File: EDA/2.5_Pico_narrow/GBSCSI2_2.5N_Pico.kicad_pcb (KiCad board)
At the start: 4 copper layers, 69.5 x 93.5 mm, 109 parts, among them J1 SCSI_50-2P_2mm, J1.1 SCSI_50P_2.54mm, J2 TF003, J5 Conn_01x04, J6 Conn_01x02, Q1 AO3401A, Q10 AO3401A, Q11 AO3401A, Q12 AO3401A, Q13 AO3401A, Q14 AO3401A, Q15 AO3401A, Q16 AO3401A, Q17 AO3401A, Q18 AO3401A, Q2 AO3401A, Q3 AO3401A, Q4 AO3401A, Q5 AO3401A, Q6 AO3401A, Q7 AO3401A, Q8 AO3401A, Q9 AO3401A, SW1 SW_DIP_x03, U1 Pico(2(W)), U10 AZ1117-2.85, U4 74LVTH245, U5 74LVTH245, U6 74LVTH125, U7 74LVTH125, U8 SN74AHC1G125DBVR, U9 TLV62569DBV

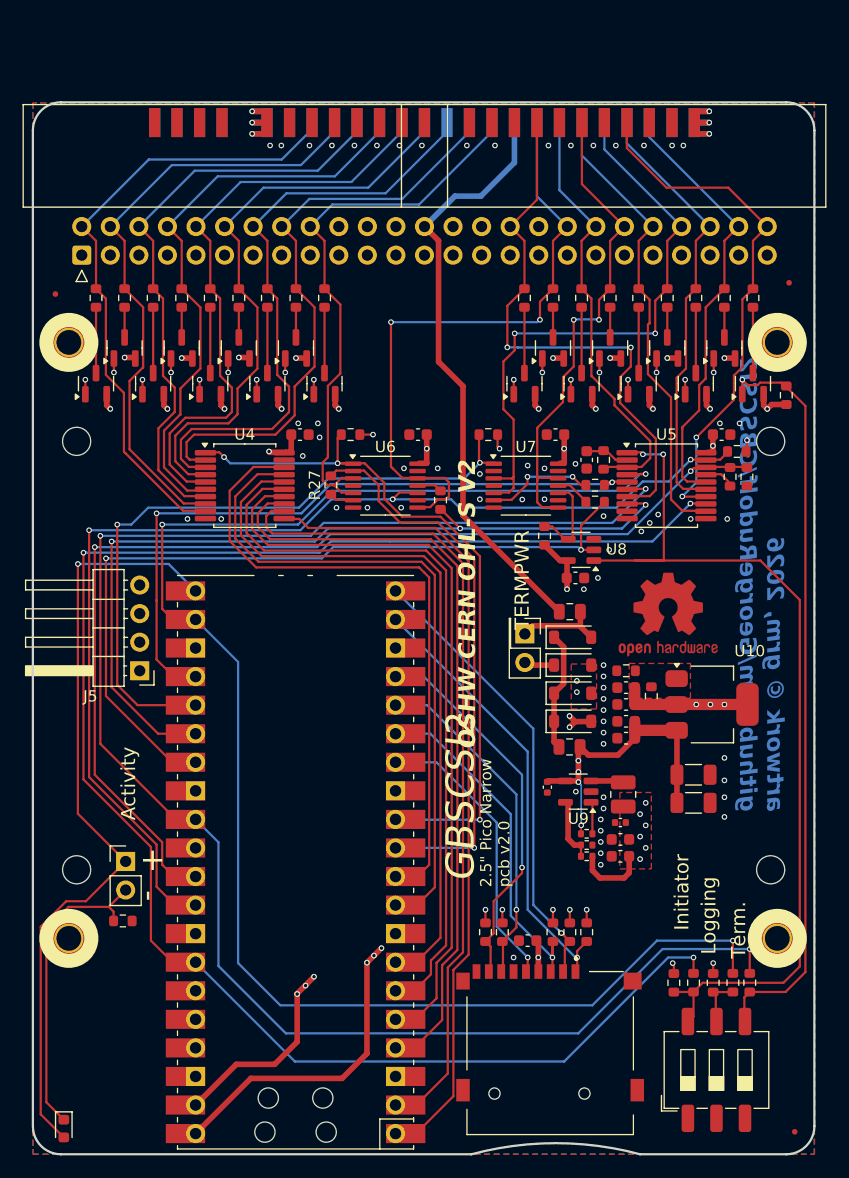
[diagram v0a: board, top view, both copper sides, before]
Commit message: Tidying up PCB footprint slightly, more work needed, ERC passes on narrow variants
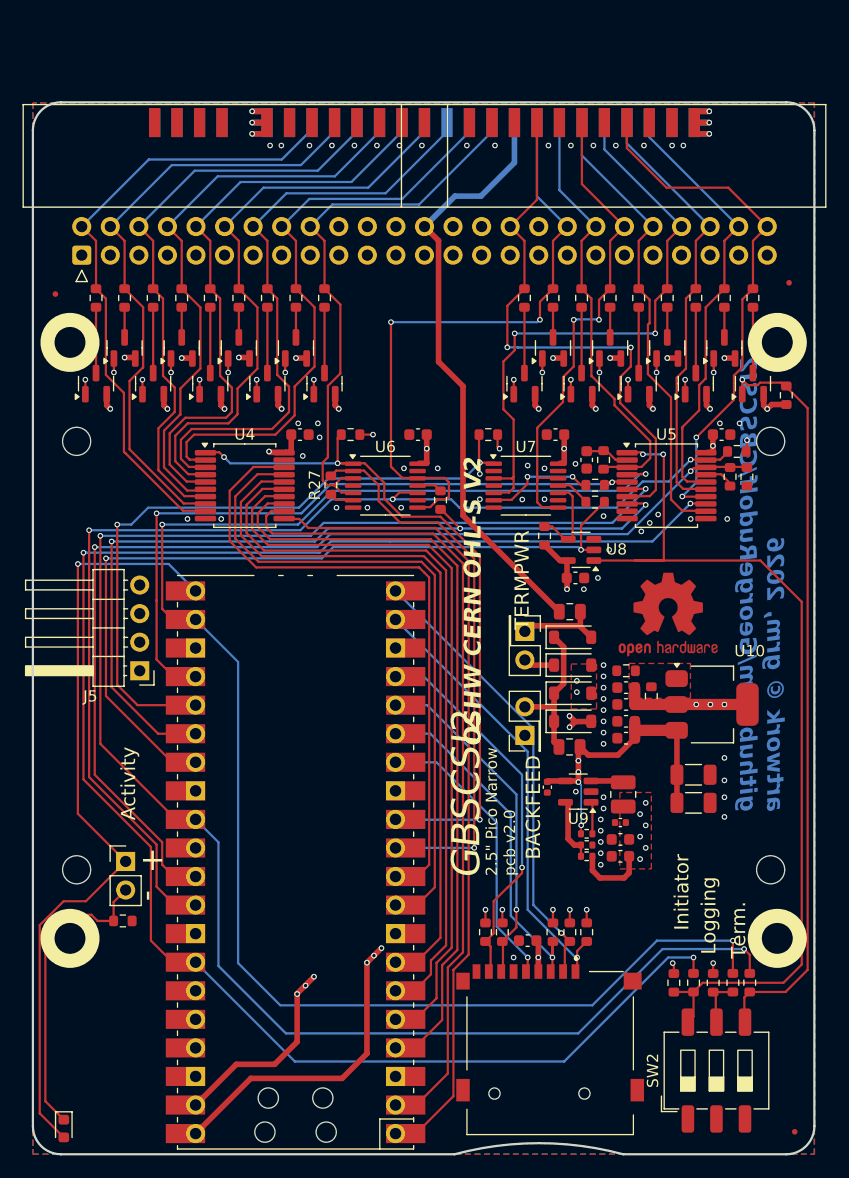
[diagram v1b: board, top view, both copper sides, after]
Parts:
- removed SW1: SW_DIP_x03, Button_Switch_SMD:SW_DIP_SPSTx03_Slide_6.7x9.18mm_W8.61mm_P2.54mm_LowProfile
- added JP2: Jumper_2_Open, Connector_PinHeader_2.54mm:PinHeader_2x01_P2.54mm_Vertical, F.Cu at (79.2, 105.2)
- added SW2: SW_DIP_x03, Button_Switch_SMD:SW_DIP_SPSTx03_Slide_6.7x9.18mm_W8.61mm_P2.54mm_LowProfile, F.Cu at (96.3, 135.1)
- R10, R11, R12, R5, R6, R8, R9: value 4k7 -> 4.7kΩ
- moved JP1 0.22 mm to (79.2, 96.0)
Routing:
- net +5VIN: track 282.0 -> 291.1 mm
- net /Power/5V_TIE: track 10.6 -> 13.3 mm
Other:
- outline, holes or cut-outs redrawn
- board text added: "BACKFEED"

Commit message: Prettifying models
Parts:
- moved C20 7.00 mm to (94.2, 104.2)
- moved C21 7.00 mm to (84.8, 73.8)
- moved C22 7.00 mm to (59.2, 71.5)
- moved C23 7.00 mm to (96.8, 71.5)
- moved C24 7.00 mm to (83.8, 84.2)
- moved C25 7.00 mm to (69.8, 71.5)
- moved C26 7.00 mm to (82.0, 71.5)
- moved C27 7.00 mm to (81.2, 102.9)
- moved C28 7.00 mm to (87.8, 106.0)
- moved C29 7.00 mm to (87.8, 109.0)
- moved C30 7.00 mm to (87.8, 107.5)
- moved C31 7.00 mm to (88.2, 98.5)
- moved C32 7.00 mm to (88.2, 97.0)
- moved C33 7.00 mm to (88.2, 95.5)
- moved C34 7.00 mm to (88.2, 94.0)
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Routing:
- net +5VIN: track 291.1 -> 181.3 mm
- net +2.8V: track 192.5 -> 181.3 mm
- net GND: track 0.00 -> 7.85 mm
- net /Core Logic, Basic Controls/~{MCU_REQ}: track 140.2 -> 144.5 mm
- net VBUS: track 76.8 -> 78.6 mm
- net /Core Logic, Basic Controls/SDIO_D3: track 40.4 -> 42.0 mm
- net /Core Logic, Basic Controls/~{MCU_IO}: track 150.1 -> 149.1 mm
- net /Core Logic, Basic Controls/~{MCU_ATTN}: track 152.3 -> 153.1 mm
- added copper zone on B.Cu, net +3.3V
- added copper zone on In2.Cu, net GND
- removed copper zone on In2.Cu, net +3.3V
- removed copper zone on B.Cu, net GND

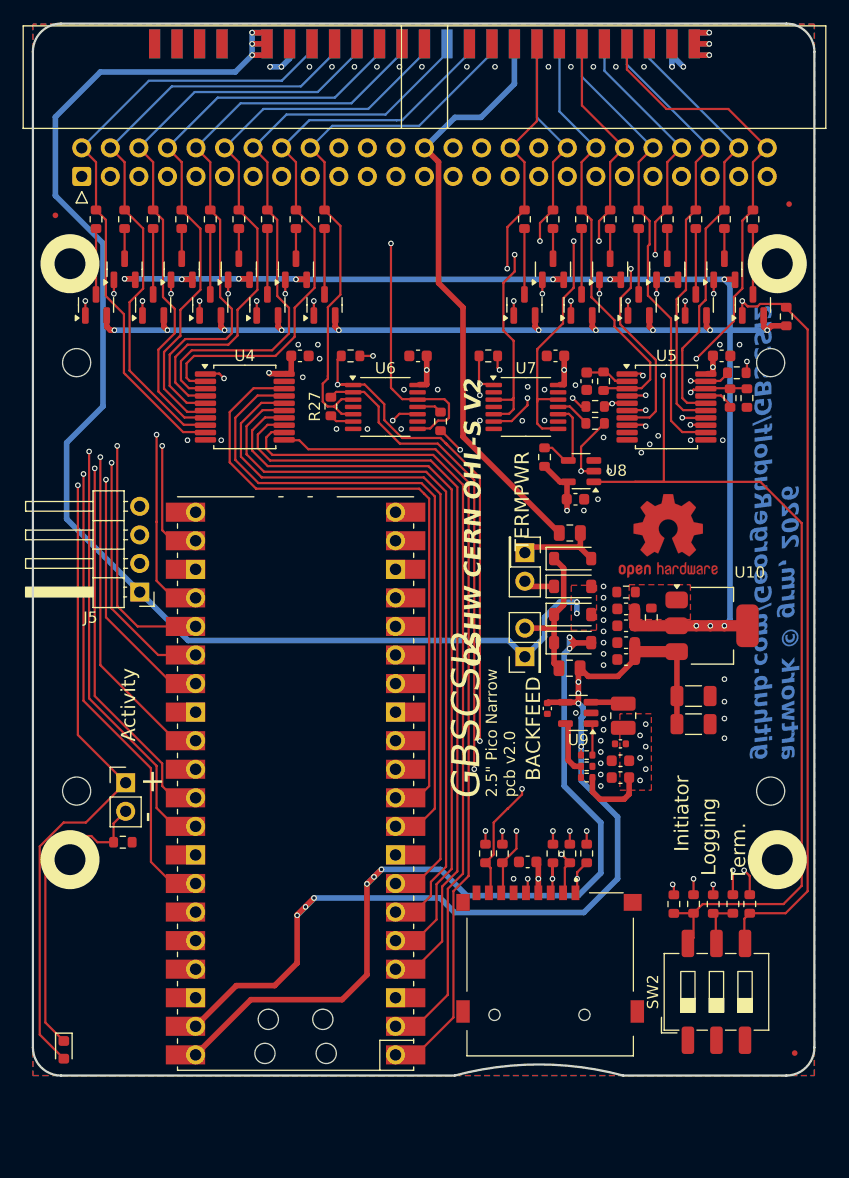
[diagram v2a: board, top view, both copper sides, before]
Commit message: Fixing PCB footprint
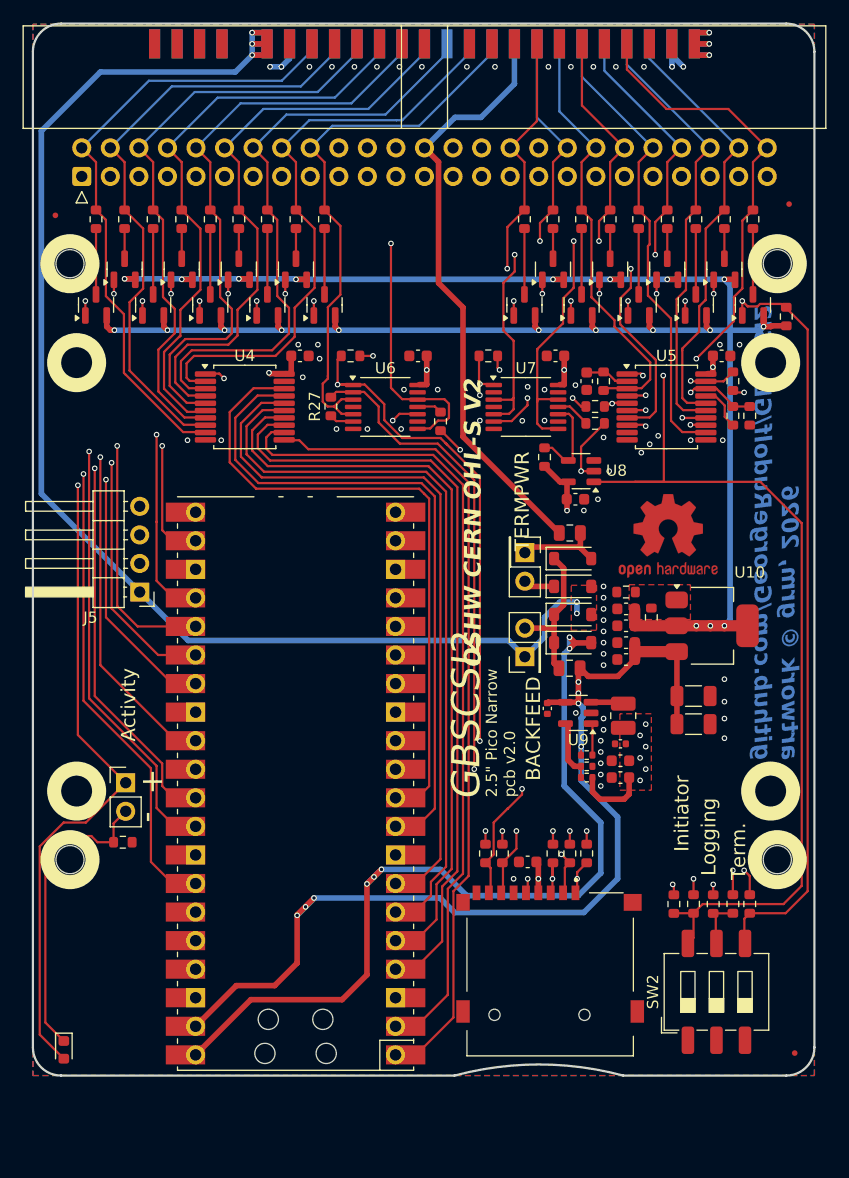
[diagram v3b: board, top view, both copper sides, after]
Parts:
- moved R17 1.59 mm to (99.2, 76.8)
- moved R26 1.59 mm to (97.8, 76.8)
- moved R6 0.83 mm to (97.8, 73.8), turned to 90 degrees
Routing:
- net Net-(U5-B1): track 2.33 -> 4.07 mm
- net +5VIN: track 181.3 -> 179.7 mm
- net /Core Logic, Basic Controls/~{MCU_ACK}: track 95.1 -> 96.1 mm
- net /Core Logic, Basic Controls/~{MCU_BSY_OUT}: track 101.3 -> 102.0 mm
